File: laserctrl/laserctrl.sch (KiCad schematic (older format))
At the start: 17 parts

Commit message: Added a todo list so I don't forget the last bits and tried annotating different ways
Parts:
- gave numbers to parts that had none: 17
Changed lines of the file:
@@
-EESchema Schematic File Version 2  date 2011-11-06T20:55:52 CET
+EESchema Schematic File Version 2  date 2011-11-06T22:48:15 CET
 LIBS:power
 LIBS:device
@@
 $EndDescr
 Wire Wire Line
+	9100 1500 9000 1500
+Wire Wire Line
+	9100 1300 9000 1300
+Wire Wire Line
+	9100 1100 9000 1100
+Wire Wire Line
+	9100 900  9000 900
+Wire Wire Line
+	8050 1900 8150 1900
+Wire Wire Line
+	8050 1600 8150 1600
+Wire Wire Line
+	8050 1400 8150 1400
+Wire Wire Line
+	8050 1100 8150 1100
+Wire Wire Line
+	8050 800  8150 800
+Wire Wire Line
+	10200 1850 10100 1850
+Wire Wire Line
+	10200 4550 10100 4550
+Wire Wire Line
 	5500 900  5600 900
 Wire Wire Line
@@
 Wire Wire Line
 	5600 800  5500 800
+Wire Wire Line
+	10200 5850 10100 5850
+Wire Wire Line
+	10200 3200 10100 3200
+Wire Wire Line
+	8150 3650 8050 3650
+Wire Wire Line
+	8150 900  8050 900
+Wire Wire Line
+	8150 1300 8050 1300
+Wire Wire Line
+	8150 1500 8050 1500
+Wire Wire Line
+	8150 1800 8050 1800
+Wire Wire Line
+	9000 800  9100 800
+Wire Wire Line
+	9000 1000 9100 1000
+Wire Wire Line
+	9000 1200 9100 1200
+Wire Wire Line
+	9000 1400 9100 1400
+Text GLabel 9100 1500 2    50   Input ~ 0
+P2.12
+Text GLabel 9100 1400 2    50   Input ~ 0
+P2.11
+Text GLabel 9100 1200 2    50   Input ~ 0
+P2.4
+Text GLabel 9100 1300 2    50   Input ~ 0
+P2.3
+Text GLabel 9100 1000 2    50   Input ~ 0
+P2.9
+Text GLabel 9100 1100 2    50   Input ~ 0
+P2.8
+Text GLabel 9100 900  2    50   Input ~ 0
+P0.18
+Text GLabel 9100 800  2    50   Input ~ 0
+P0.19
+Text GLabel 8050 1100 0    50   Input ~ 0
+P1.19
+Text GLabel 8050 3650 0    50   Input ~ 0
+WDLE
+Text GLabel 8050 1900 0    50   Input ~ 0
+WDLE
+Text GLabel 10100 5850 0    50   Input ~ 0
+WDME
+Text GLabel 10100 4550 0    50   Input ~ 0
+WDME
+Text GLabel 10100 3200 0    50   Input ~ 0
+WDME
+Text GLabel 10100 1850 0    50   Input ~ 0
+WDME
+Text GLabel 8050 1800 0    50   Input ~ 0
+WDME
+Text GLabel 8050 1600 0    50   Input ~ 0
+P2.0
+Text GLabel 8050 1500 0    50   Input ~ 0
+P2.5
+Text GLabel 8050 1400 0    50   Input ~ 0
+P0.16
+Text GLabel 8050 1300 0    50   Input ~ 0
+P0.21
 Text Notes 5050 5000 0    50   ~ 0
 Supply voltage sense (10.8696 %)
@@
 AD5
 $Comp
-L AGND #PWR?
+L AGND #PWR8
 U 1 1 4EB471B3
 P 2850 7450
-F 0 "#PWR?" H 2850 7450 40  0001 C CNN
+F 0 "#PWR8" H 2850 7450 40  0001 C CNN
 F 1 "AGND" H 2850 7380 50  0000 C CNN
 	1    2850 7450
@@
 $EndComp
 $Comp
-L GND #PWR?
+L GND #PWR7
 U 1 1 4EB47172
 P 2550 7450
-F 0 "#PWR?" H 2550 7450 30  0001 C CNN
+F 0 "#PWR7" H 2550 7450 30  0001 C CNN
 F 1 "GND" H 2550 7380 30  0001 C CNN
 	1    2550 7450
@@
 TXD0
 $Comp
-L C C?
+L C C1
 U 1 1 4EAD4B80
 P 7050 6650
-F 0 "C?" H 7100 6750 50  0000 L CNN
+F 0 "C1" H 7100 6750 50  0000 L CNN
 F 1 "10nF" H 7100 6550 50  0000 L CNN
 	1    7050 6650
@@
 $EndComp
 $Comp
-L R R?
+L R R1
 U 1 1 4EA467FA
 P 7050 5400
-F 0 "R?" V 7130 5400 50  0000 C CNN
+F 0 "R1" V 7130 5400 50  0000 C CNN
 F 1 "10k" V 7050 5400 50  0000 C CNN
 	1    7050 5400
@@
 $EndComp
 $Comp
-L R R?
+L R R2
 U 1 1 4EAD4A29
 P 7200 5400
-F 0 "R?" V 7280 5400 50  0000 C CNN
+F 0 "R2" V 7280 5400 50  0000 C CNN
 F 1 "R" V 7200 5400 50  0000 C CNN
 	1    7200 5400
@@
 F6 "STEP" I L 10200 5250 60
 F7 "~ENABLE" I L 10200 4950 60
+F8 "~RESET" I L 10200 5850 60
 $EndSheet
 $Sheet
@@
 F6 "Current" I L 10200 2750 60
 F7 "Min-Limit" O L 10200 3050 60
+F8 "~RESET" I L 10200 3200 60
 $EndSheet
 $Comp
-L R R?
+L R R7
 U 1 1 4EA468B0
 P 7500 6700
-F 0 "R?" V 7580 6700 50  0000 C CNN
+F 0 "R7" V 7580 6700 50  0000 C CNN
 F 1 "10k" V 7500 6700 50  0000 C CNN
 	1    7500 6700
@@
 $EndComp
 $Comp
-L R R?
+L R R8
 U 1 1 4EA468A6
 P 7650 6700
-F 0 "R?" V 7730 6700 50  0000 C CNN
+F 0 "R8" V 7730 6700 50  0000 C CNN
 F 1 "10k" V 7650 6700 50  0000 C CNN
 	1    7650 6700
@@
 $EndComp
 $Comp
-L R R?
+L R R3
 U 1 1 4EA46801
 P 7350 5400
-F 0 "R?" V 7430 5400 50  0000 C CNN
+F 0 "R3" V 7430 5400 50  0000 C CNN
 F 1 "10k" V 7350 5400 50  0000 C CNN
 	1    7350 5400
@@
 $EndComp
 $Comp
-L R R?
+L R R4
 U 1 1 4EA467F5
 P 7500 5400
-F 0 "R?" V 7580 5400 50  0000 C CNN
+F 0 "R4" V 7580 5400 50  0000 C CNN
 F 1 "10k" V 7500 5400 50  0000 C CNN
 	1    7500 5400
@@
 $EndComp
 $Comp
-L R R?
+L R R5
 U 1 1 4EA467E7
 P 7650 5400
-F 0 "R?" V 7730 5400 50  0000 C CNN
+F 0 "R5" V 7730 5400 50  0000 C CNN
 F 1 "10k" V 7650 5400 50  0000 C CNN
 	1    7650 5400
@@
 ~TRST
 $Comp
-L +3.3V #PWR?
+L +3.3V #PWR1
 U 1 1 4EA46529
 P 8900 5075
-F 0 "#PWR?" H 8900 5035 30  0001 C CNN
+F 0 "#PWR1" H 8900 5035 30  0001 C CNN
 F 1 "+3.3V" H 8900 5185 30  0000 C CNN
 	1    8900 5075
@@
 $EndComp
 $Comp
-L GND #PWR?
+L GND #PWR2
 U 1 1 4EA464E3
 P 8900 7050
-F 0 "#PWR?" H 8900 7050 30  0001 C CNN
+F 0 "#PWR2" H 8900 7050 30  0001 C CNN
 F 1 "GND" H 8900 6980 30  0001 C CNN
 	1    8900 7050
@@
 $EndComp
 $Comp
-L CONN_10X2 P?
+L CONN_10X2 P1
 U 1 1 4EA464D4
 P 8350 6100
-F 0 "P?" H 8350 6650 60  0000 C CNN
+F 0 "P1" H 8350 6650 60  0000 C CNN
 F 1 "JTAG" V 8350 6000 50  0000 C CNN
 	1    8350 6100
@@
 TDO
 $Comp
-L GND #PWR?
+L GND #PWR6
 U 1 1 4EA3EE94
 P 6325 7375
-F 0 "#PWR?" H 6325 7375 30  0001 C CNN
+F 0 "#PWR6" H 6325 7375 30  0001 C CNN
 F 1 "GND" H 6325 7305 30  0001 C CNN
 	1    6325 7375
@@
 $EndComp
 $Comp
-L GND #PWR?
+L GND #PWR5
 U 1 1 4EA3EE90
 P 5700 7375
-F 0 "#PWR?" H 5700 7375 30  0001 C CNN
+F 0 "#PWR5" H 5700 7375 30  0001 C CNN
 F 1 "GND" H 5700 7305 30  0001 C CNN
 	1    5700 7375
@@
 $EndComp
 $Comp
-L GND #PWR?
+L GND #PWR4
 U 1 1 4EA3EE8C
 P 5450 7375
-F 0 "#PWR?" H 5450 7375 30  0001 C CNN
+F 0 "#PWR4" H 5450 7375 30  0001 C CNN
 F 1 "GND" H 5450 7305 30  0001 C CNN
 	1    5450 7375
@@
 $EndComp
 $Comp
-L GND #PWR?
+L GND #PWR3
 U 1 1 4EA3EE86
 P 4775 7375
-F 0 "#PWR?" H 4775 7375 30  0001 C CNN
+F 0 "#PWR3" H 4775 7375 30  0001 C CNN
 F 1 "GND" H 4775 7305 30  0001 C CNN
 	1    4775 7375
@@
 $EndComp
 $Comp
-L C C?
+L C C5
 U 1 1 4EA3EE6C
 P 6325 7075
-F 0 "C?" H 6375 7175 50  0000 L CNN
+F 0 "C5" H 6375 7175 50  0000 L CNN
 F 1 "5pF" H 6375 6975 50  0000 L CNN
 	1    6325 7075
@@
 $EndComp
 $Comp
-L C C?
+L C C4
 U 1 1 4EA3EE66
 P 5700 7075
-F 0 "C?" H 5750 7175 50  0000 L CNN
+F 0 "C4" H 5750 7175 50  0000 L CNN
 F 1 "5pF" H 5750 6975 50  0000 L CNN
 	1    5700 7075
@@
 $EndComp
 $Comp
-L C C?
+L C C3
 U 1 1 4EA3EE5C
 P 5450 7075
-F 0 "C?" H 5500 7175 50  0000 L CNN
+F 0 "C3" H 5500 7175 50  0000 L CNN
 F 1 "15pF" H 5500 6975 50  0000 L CNN
 	1    5450 7075
@@
 $EndComp
 $Comp
-L C C?
+L C C2
 U 1 1 4EA3EE55
 P 4775 7075
-F 0 "C?" H 4825 7175 50  0000 L CNN
+F 0 "C2" H 4825 7175 50  0000 L CNN
 F 1 "18pF" H 4825 6975 50  0000 L CNN
 	1    4775 7075
@@
 $EndComp
 $Comp
-L R R?
+L R R6
 U 1 1 4EA3EE02
 P 5100 6650
-F 0 "R?" V 5180 6650 50  0000 C CNN
+F 0 "R6" V 5180 6650 50  0000 C CNN
 F 1 "100k" V 5100 6650 50  0000 C CNN
 	1    5100 6650
@@
 $EndComp
 $Comp
-L CRYSTAL X?
+L CRYSTAL X1
 U 1 1 4EA3EDBB
 P 5150 6450
-F 0 "X?" H 5225 6625 60  0000 C CNN
+F 0 "X1" H 5225 6625 60  0000 C CNN
 F 1 "12MHz" H 5425 6525 60  0000 C CNN
 	1    5150 6450
@@
 $EndComp
 $Comp
-L CRYSTAL X?
+L CRYSTAL X2
 U 1 1 4EA3EDAF
 P 6025 6750
-F 0 "X?" H 6025 6900 60  0000 C CNN
+F 0 "X2" H 6025 6900 60  0000 C CNN
 F 1 "32768Hz" H 6025 6600 60  0000 C CNN
 	1    6025 6750
@@
 $EndComp
 $Comp
-L +BATT #PWR?
+L +BATT #PWR11
 U 1 1 4EA3ED82
 P 4100 7450
-F 0 "#PWR?" H 4100 7400 20  0001 C CNN
+F 0 "#PWR11" H 4100 7400 20  0001 C CNN
 F 1 "+BATT" H 4100 7550 30  0000 C CNN
 	1    4100 7450
@@
 $EndComp
 $Comp
-L +3.3VADC #PWR?
+L +3.3VADC #PWR10
 U 1 1 4EA3EA65
 P 3800 7450
-F 0 "#PWR?" H 3800 7570 20  0001 C CNN
+F 0 "#PWR10" H 3800 7570 20  0001 C CNN
 F 1 "+3.3VADC" H 3800 7540 30  0000 C CNN
 	1    3800 7450
@@
 $EndComp
 $Comp
-L +3.3V #PWR?
+L +3.3V #PWR9
 U 1 1 4EA3EA51
 P 3400 7450
-F 0 "#PWR?" H 3400 7410 30  0001 C CNN
+F 0 "#PWR9" H 3400 7410 30  0001 C CNN
 F 1 "+3.3V" H 3400 7560 30  0000 C CNN
 	1    3400 7450
@@
 $EndComp
 $Comp
-L LPC1769FBD100 U?
+L LPC1769FBD100 U1
 U 1 1 4EA3E54B
 P 3150 4900
-F 0 "U?" H 1850 7500 60  0000 C CNN
+F 0 "U1" H 1850 7500 60  0000 C CNN
 F 1 "LPC1769FBD100" H 2150 7400 60  0000 C CNN
 	1    3150 4900
@@
 $EndComp
 $Sheet
-S 8150 700  975  1675
+S 8150 700  850  1300
 U 4EA3E488
 F0 "watchdog" 60
 F1 "watchdog.sch" 60
+F2 "Enable Motors" O L 8150 1800 60
+F3 "Enable LASER" O L 8150 1900 60
+F4 "Amin" I R 9000 1500 60
+F5 "Amax" I R 9000 1400 60
+F6 "Zmax" I R 9000 1200 60
+F7 "Zmin" I R 9000 1300 60
+F8 "Ymax" I R 9000 1000 60
+F9 "Ymin" I R 9000 1100 60
+F10 "Xmin" I R 9000 900 60
+F11 "Xmax" I R 9000 800 60
+F12 "FIRE" I L 8150 1100 60
+F13 "Astep" I L 8150 1600 60
+F14 "Zstep" I L 8150 1500 60
+F15 "Ystep" I L 8150 1400 60
+F16 "Xstep" I L 8150 1300 60
+F17 "RXD" I L 8150 800 60
+F18 "TXD" O L 8150 900 60
 $EndSheet
 $Sheet
@@
 F6 "Current" I L 10200 4100 60
 F7 "Min-Limit" O L 10200 4400 60
+F8 "~RESET" I L 10200 4550 60
 $EndSheet
 $Sheet
@@
 F6 "Current" I L 10200 1400 60
 F7 "Min-Limit" O L 10200 1700 60
+F8 "~RESET" I L 10200 1850 60
 $EndSheet
 $Sheet

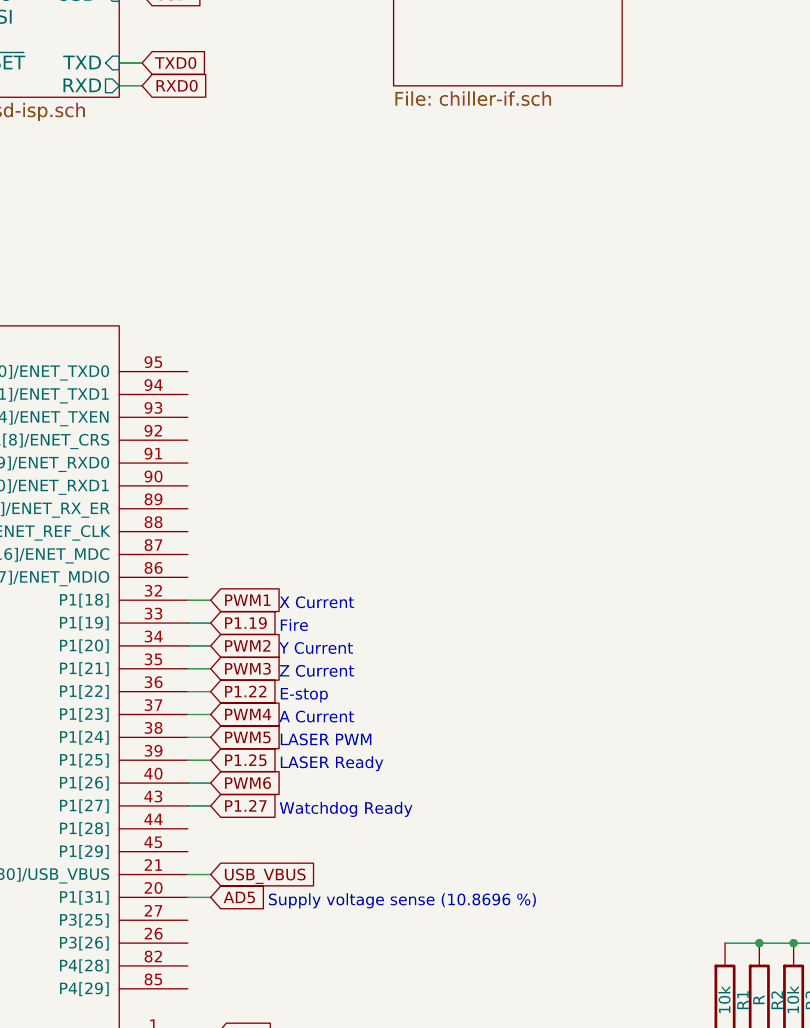
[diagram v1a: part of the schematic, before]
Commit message: Added relay drivers for exhaust and assist air
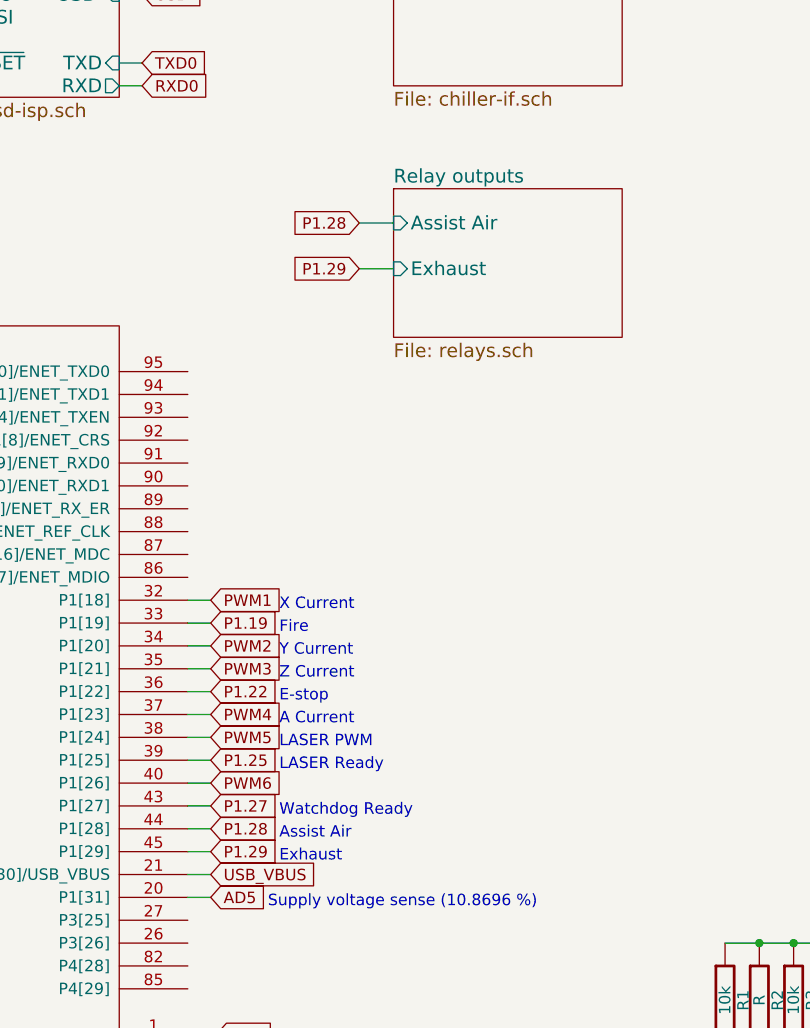
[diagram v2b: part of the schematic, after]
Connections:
- net P1.28: now reaches U1.44 (P1[28])
- net P1.29: now reaches U1.45 (P1[29])
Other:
- note added: "Assist Air"
- note added: "Exhaust"
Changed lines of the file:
@@
-EESchema Schematic File Version 2  date 2011-11-06T22:48:15 CET
+EESchema Schematic File Version 2  date 2011-11-07T20:42:45 CET
 LIBS:power
 LIBS:device
@@
 $Descr A4 11700 8267
 encoding utf-8
-Sheet 1 11
+Sheet 1 12
 Title ""
-Date "6 nov 2011"
+Date "7 nov 2011"
 Rev ""
 Comp ""
@@
 Comment4 ""
 $EndDescr
+Text Notes 5100 4800 0    50   ~ 0
+Exhaust
+Text Notes 5100 4700 0    50   ~ 0
+Assist Air
+Wire Wire Line
+	5600 2000 5450 2000
+Wire Wire Line
+	4700 4650 4800 4650
 Wire Wire Line
 	9100 1500 9000 1500
@@
 Wire Wire Line
 	9000 1400 9100 1400
+Wire Wire Line
+	4800 4750 4700 4750
+Wire Wire Line
+	5450 2200 5600 2200
+Text GLabel 5450 2000 0    50   Input ~ 0
+P1.28
+Text GLabel 5450 2200 0    50   Input ~ 0
+P1.29
+Text GLabel 4800 4750 2    50   Input ~ 0
+P1.29
+Text GLabel 4800 4650 2    50   Input ~ 0
+P1.28
+$Sheet
+S 5600 1850 1000 650
+U 4EB82FA9
+F0 "Relay outputs" 60
+F1 "relays.sch" 60
+F2 "Assist Air" I L 5600 2000 60
+F3 "Exhaust" I L 5600 2200 60
+$EndSheet
 Text GLabel 9100 1500 2    50   Input ~ 0
 P2.12

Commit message: Started some cleaning up
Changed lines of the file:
@@
-EESchema Schematic File Version 2  date 2011-11-08T22:27:11 CET
+EESchema Schematic File Version 2  date 2011-11-09T19:37:00 CET
 LIBS:power
 LIBS:device
@@
 LIBS:atmel
 LIBS:microsd
-LIBS:laserctrl-cache
+LIBS:jumper3
 EELAYER 25  0
 EELAYER END
 $Descr A4 11700 8267
 encoding utf-8
-Sheet 1 12
+Sheet 1 10
 Title ""
-Date "8 nov 2011"
+Date "9 nov 2011"
 Rev ""
 Comp ""
@@
 Comment4 ""
 $EndDescr
-Text Notes 5100 4800 0    50   ~ 0
-Exhaust
-Text Notes 5100 4700 0    50   ~ 0
-Assist Air
-Wire Wire Line
-	5600 2000 5450 2000
+Wire Wire Line
+	6800 1600 6700 1600
+Wire Wire Line
+	5850 1900 5950 1900
 Wire Wire Line
 	4700 4650 4800 4650
@@
 	10200 4550 10100 4550
 Wire Wire Line
-	5500 900  5600 900
-Wire Wire Line
-	3550 1100 3650 1100
-Wire Wire Line
-	3550 900  3650 900
-Wire Wire Line
-	4500 1300 4400 1300
-Wire Wire Line
-	3550 1400 3650 1400
-Wire Wire Line
-	4400 1000 4500 1000
-Wire Wire Line
-	4400 800  4500 800
+	5850 1100 5950 1100
+Wire Wire Line
+	5850 900  5950 900
+Wire Wire Line
+	6800 1300 6700 1300
+Wire Wire Line
+	5850 1400 5950 1400
+Wire Wire Line
+	6700 1000 6800 1000
+Wire Wire Line
+	6700 800  6800 800
 Wire Wire Line
 	1500 3750 1400 3750
@@
 	10100 6250 10200 6250
 Wire Wire Line
-	4500 900  4400 900
-Wire Wire Line
-	3550 1300 3650 1300
-Wire Wire Line
-	4400 1400 4500 1400
-Wire Wire Line
-	3650 800  3550 800
-Wire Wire Line
-	3650 1000 3550 1000
-Wire Wire Line
-	5600 800  5500 800
+	6800 900  6700 900
+Wire Wire Line
+	5850 1300 5950 1300
+Wire Wire Line
+	6700 1400 6800 1400
+Wire Wire Line
+	5950 800  5850 800
+Wire Wire Line
+	5950 1000 5850 1000
 Wire Wire Line
 	10200 5850 10100 5850
@@
 	4800 4750 4700 4750
 Wire Wire Line
-	5450 2200 5600 2200
-Text GLabel 5450 2000 0    50   Input ~ 0
+	5850 1800 5950 1800
+Wire Wire Line
+	6700 1700 6800 1700
+Text Notes 5100 4800 0    50   ~ 0
+Exhaust
+Text Notes 5100 4700 0    50   ~ 0
+Assist Air
+Text GLabel 6800 1600 2    50   Input ~ 0
 P1.28
-Text GLabel 5450 2200 0    50   Input ~ 0
+Text GLabel 6800 1700 2    50   Input ~ 0
 P1.29
 Text GLabel 4800 4750 2    50   Input ~ 0
@@
 Text GLabel 4800 4650 2    50   Input ~ 0
 P1.28
-$Sheet
-S 5600 1850 1000 650
-U 4EB82FA9
-F0 "Relay outputs" 60
-F1 "relays.sch" 60
-F2 "Assist Air" I L 5600 2000 60
-F3 "Exhaust" I L 5600 2200 60
-$EndSheet
 Text GLabel 9100 1500 2    50   Input ~ 0
 P2.12
@@
 Text GLabel 10100 6250 0    50   Input ~ 0
 AD5
-Text GLabel 3550 1300 0    50   Input ~ 0
+Text GLabel 5850 1300 0    50   Input ~ 0
 ~RESET
 Text Notes 1050 3550 1    50   ~ 0
@@
 Text Notes 700  2700 0    50   ~ 0
 Watchdog\nserial port
-Text GLabel 5500 800  0    50   Input ~ 0
+Text GLabel 5850 1800 0    50   Input ~ 0
 TXD2
-Text GLabel 5500 900  0    50   Input ~ 0
+Text GLabel 5850 1900 0    50   Input ~ 0
 RXD2
-$Sheet
-S 5600 700  1000 700
-U 4EB5C5C3
-F0 "Chiller Interface" 60
-F1 "chiller-if.sch" 60
-F2 "RXD" O L 5600 900 60
-F3 "TXD" I L 5600 800 60
-$EndSheet
 Text GLabel 1400 3750 0    50   Input ~ 0
 RXD2
@@
 Text GLabel 8050 800  0    50   Input ~ 0
 TXD3
-Text GLabel 3550 900  0    50   Input ~ 0
+Text GLabel 5850 900  0    50   Input ~ 0
 SCK1
-Text GLabel 3550 1000 0    50   Input ~ 0
+Text GLabel 5850 1000 0    50   Input ~ 0
 MISO1
-Text GLabel 3550 1100 0    50   Input ~ 0
+Text GLabel 5850 1100 0    50   Input ~ 0
 MOSI1
-Text GLabel 3550 800  0    50   Input ~ 0
+Text GLabel 5850 800  0    50   Input ~ 0
 SD_CS
-Text GLabel 3550 1400 0    50   Input ~ 0
+Text GLabel 5850 1400 0    50   Input ~ 0
 ~ISP
-Text GLabel 4500 1300 2    50   Input ~ 0
+Text GLabel 6800 1300 2    50   Input ~ 0
 TXD0
-Text GLabel 4500 1400 2    50   Input ~ 0
+Text GLabel 6800 1400 2    50   Input ~ 0
 RXD0
-Text GLabel 4500 1000 2    50   Input ~ 0
+Text GLabel 6800 1000 2    50   Input ~ 0
 USB-
-Text GLabel 4500 900  2    50   Input ~ 0
+Text GLabel 6800 900  2    50   Input ~ 0
 USB+
-Text GLabel 4500 800  2    50   Input ~ 0
+Text GLabel 6800 800  2    50   Input ~ 0
 USB_VBUS
 $Sheet
-S 3650 700  750  750
+S 5950 700  750  1350
 U 4EB5C316
 F0 "SD card + ISP + USB" 60
 F1 "sd-isp.sch" 60
-F2 "USB_VBUS" I R 4400 800 60
-F3 "USB-" I R 4400 1000 60
-F4 "USB+" I R 4400 900 60
-F5 "RXD" O R 4400 1400 60
-F6 "TXD" I R 4400 1300 60
-F7 "~ISP" O L 3650 1400 60
-F8 "~RESET" O L 3650 1300 60
-F9 "SCK" I L 3650 900 60
-F10 "MISO" I L 3650 1000 60
-F11 "MOSI" I L 3650 1100 60
-F12 "CS" I L 3650 800 60
+F2 "USB_VBUS" I R 6700 800 60
+F3 "USB-" I R 6700 1000 60
+F4 "USB+" I R 6700 900 60
+F5 "RXD" O R 6700 1400 60
+F6 "TXD" I R 6700 1300 60
+F7 "~ISP" O L 5950 1400 60
+F8 "~RESET" O L 5950 1300 60
+F9 "SCK" I L 5950 900 60
+F10 "MISO" I L 5950 1000 60
+F11 "MOSI" I L 5950 1100 60
+F12 "CS" I L 5950 800 60
+F13 "Exhaust" I R 6700 1600 60
+F14 "Assist Air" I R 6700 1700 60
+F15 "TXDC" I L 5950 1800 60
+F16 "RXDC" O L 5950 1900 60
 $EndSheet
 Text GLabel 10100 5550 0    50   Input ~ 0
